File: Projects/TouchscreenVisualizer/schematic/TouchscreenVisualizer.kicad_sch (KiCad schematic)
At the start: 5 parts, among them J1 Load Cell, J2 USB-Serial FTDI Cable, M1 ERM Motor, U1 STM32F072RBTx, U2 DRV2605L

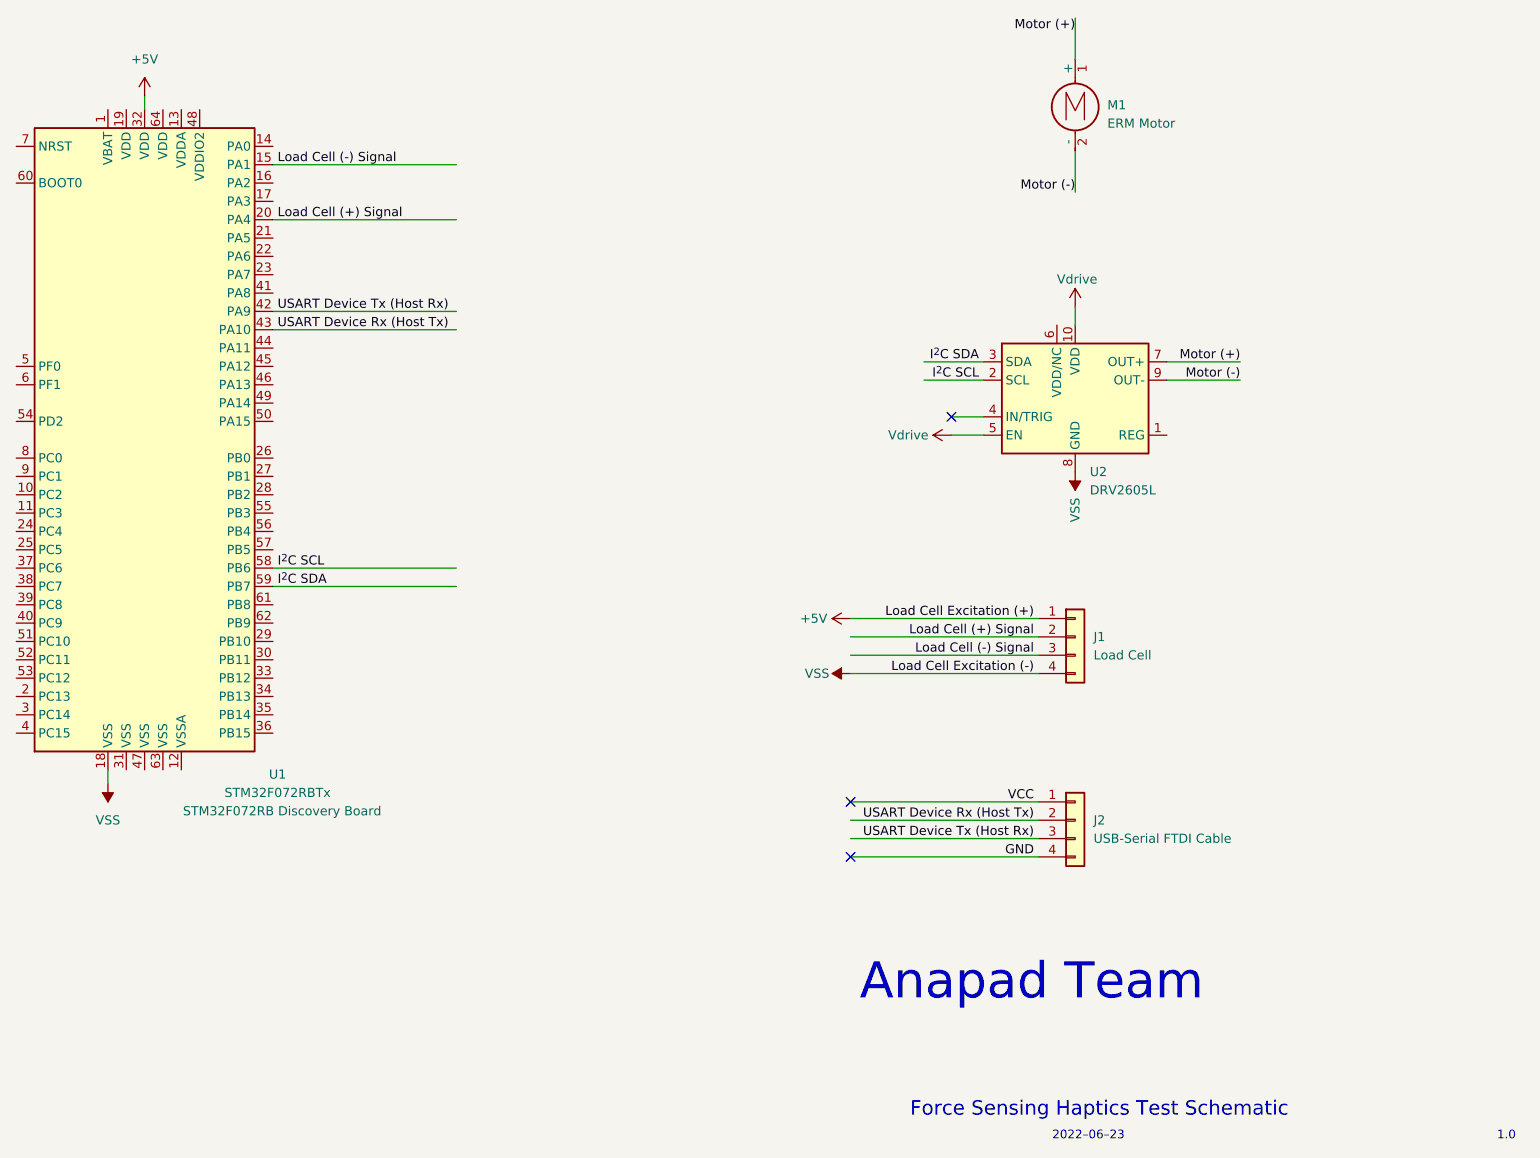
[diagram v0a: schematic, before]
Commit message: Create TouchscreenVisualizer schematic
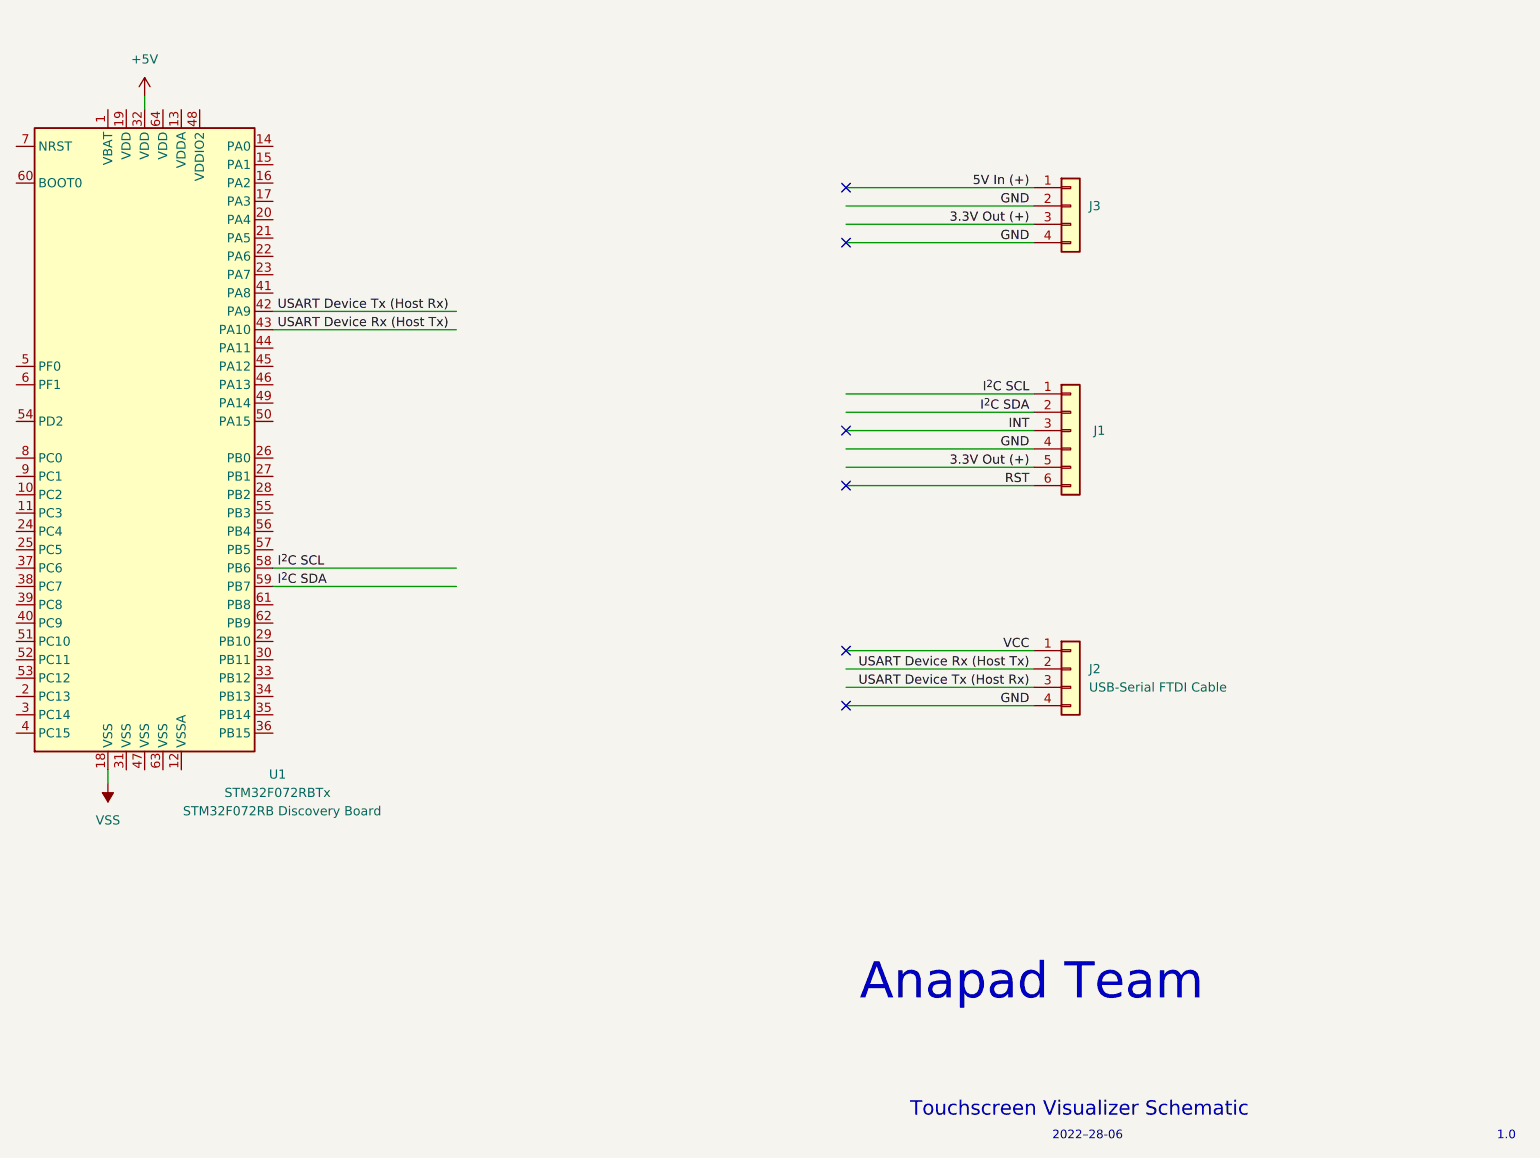
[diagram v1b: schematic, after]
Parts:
- removed J1: Load Cell, symbol Connector_Generic:Conn_01x04
- removed M1: ERM Motor, symbol Motor:Motor_DC
- removed U2: DRV2605L, Package_SO:VSSOP-10_3x3mm_P0.5mm, symbol Driver_Haptic:DRV2605LDGS
- added J1: (no value), symbol Connector_Generic:Conn_01x06
- added J3: (no value), symbol Connector_Generic:Conn_01x04
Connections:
- net GND: now also J1.4 (Pin_4), J3.2 (Pin_2), J3.4 (Pin_4)
- net I^{2}C SCL: now also J1.1 (Pin_1)
- net I^{2}C SDA: now also J1.2 (Pin_2)
- net Load Cell (+) Signal: no longer names the net of U1.20 (PA4)
- net Load Cell (-) Signal: no longer names the net of U1.15 (PA1)
- new net 3.3V Out (+): J1.5 (Pin_5), J3.3 (Pin_3)
- new net 5V In (+): J3.1 (Pin_1)
- new net INT: J1.3 (Pin_3)
- new net RST: J1.6 (Pin_6)
- no-connect marks 3 -> 6
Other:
- note added: "2022–28-06"
- note added: "Touchscreen Visualizer Schematic"
- note removed: "2022–06–23"
- note removed: "Force Sensing Haptics Test Schematic"
- moved on the sheet: J2
